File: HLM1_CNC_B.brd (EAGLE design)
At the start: 72.1 x 82.5 mm, 19 parts, among them Q1 600mA/40V, Q2 IRF540

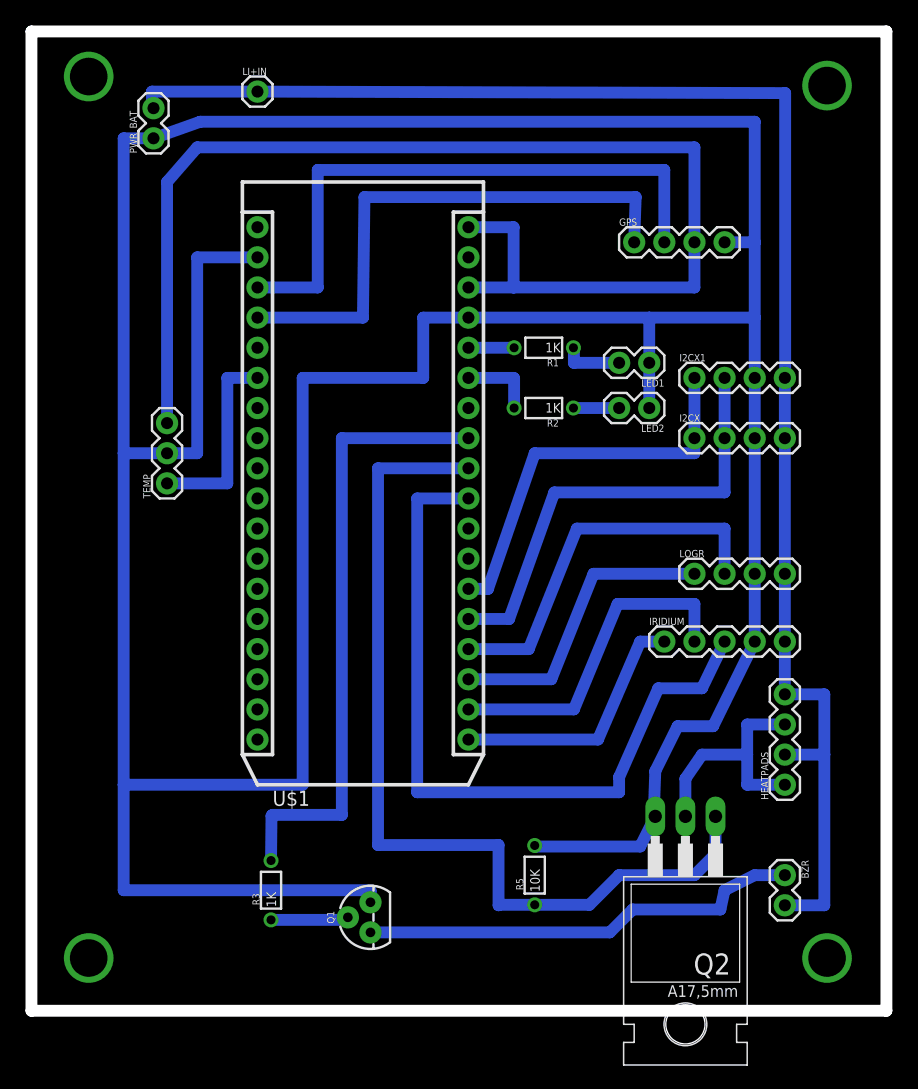
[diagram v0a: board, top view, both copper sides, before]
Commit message: Improved naming and file structure
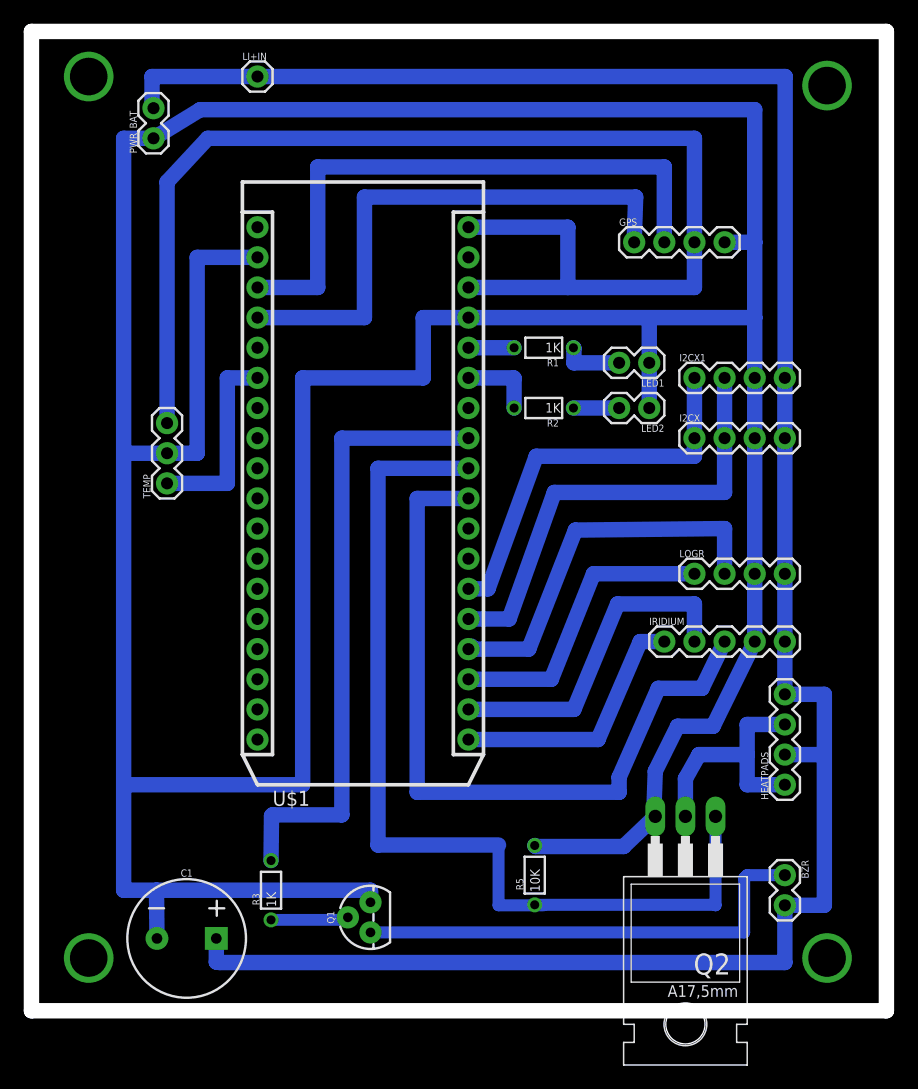
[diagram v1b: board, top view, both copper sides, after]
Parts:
- added C1: 1mF, SparkFun-Capacitors:CPOL-RADIAL-5MM-10MM
- moved LI+IN 1.27 mm to (19.1, 78.7)
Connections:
- net GND: now also C1.-
- net V_BATT: now also C1.+
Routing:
- net V_BATT: track 133.5 -> 190.9 mm
- net 3.3V: track 105.9 -> 111.5 mm
- net GND: track 344.6 -> 349.6 mm
- net D3: track 77.9 -> 81.2 mm
- net N$9: track 37.3 -> 39.6 mm
- net TX: track 50.3 -> 50.8 mm
